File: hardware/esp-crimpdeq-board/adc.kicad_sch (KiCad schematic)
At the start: 13 parts, among them IC1 ADS1235IRHBT, IC3 ADS1230IPWR

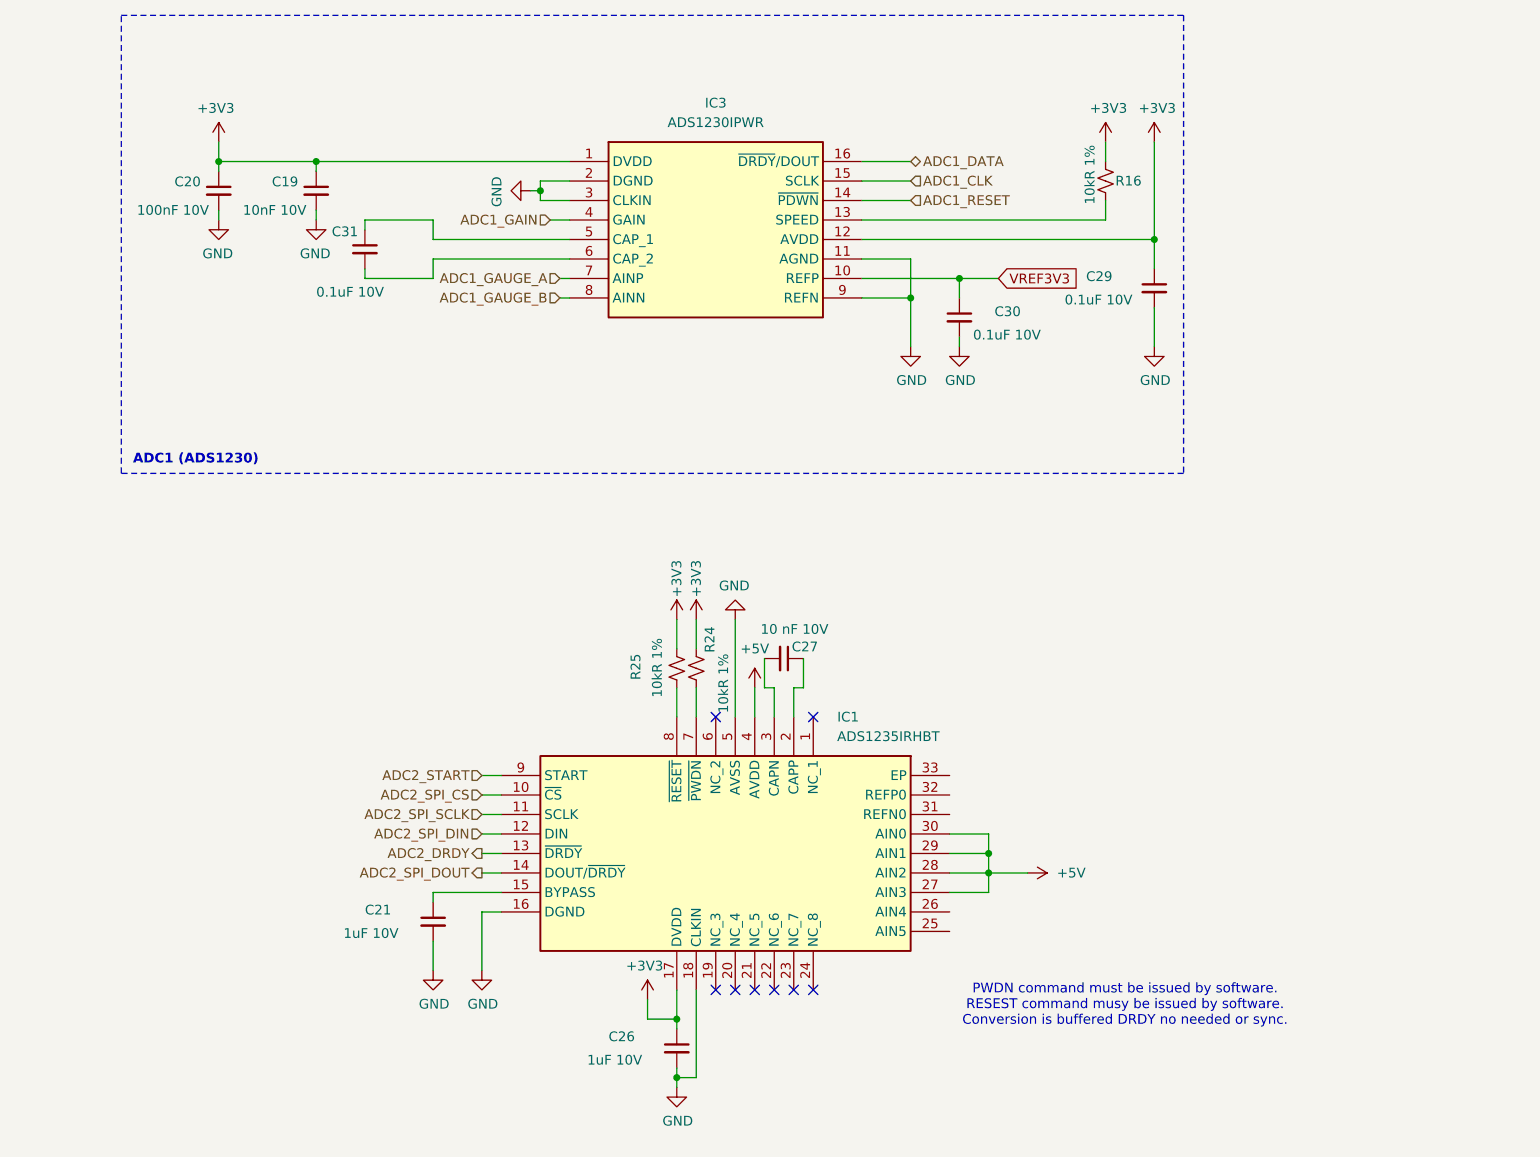
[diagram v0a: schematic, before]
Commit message: Cleaned schematic
- Pending connectors
- Pending BOM and footprints review
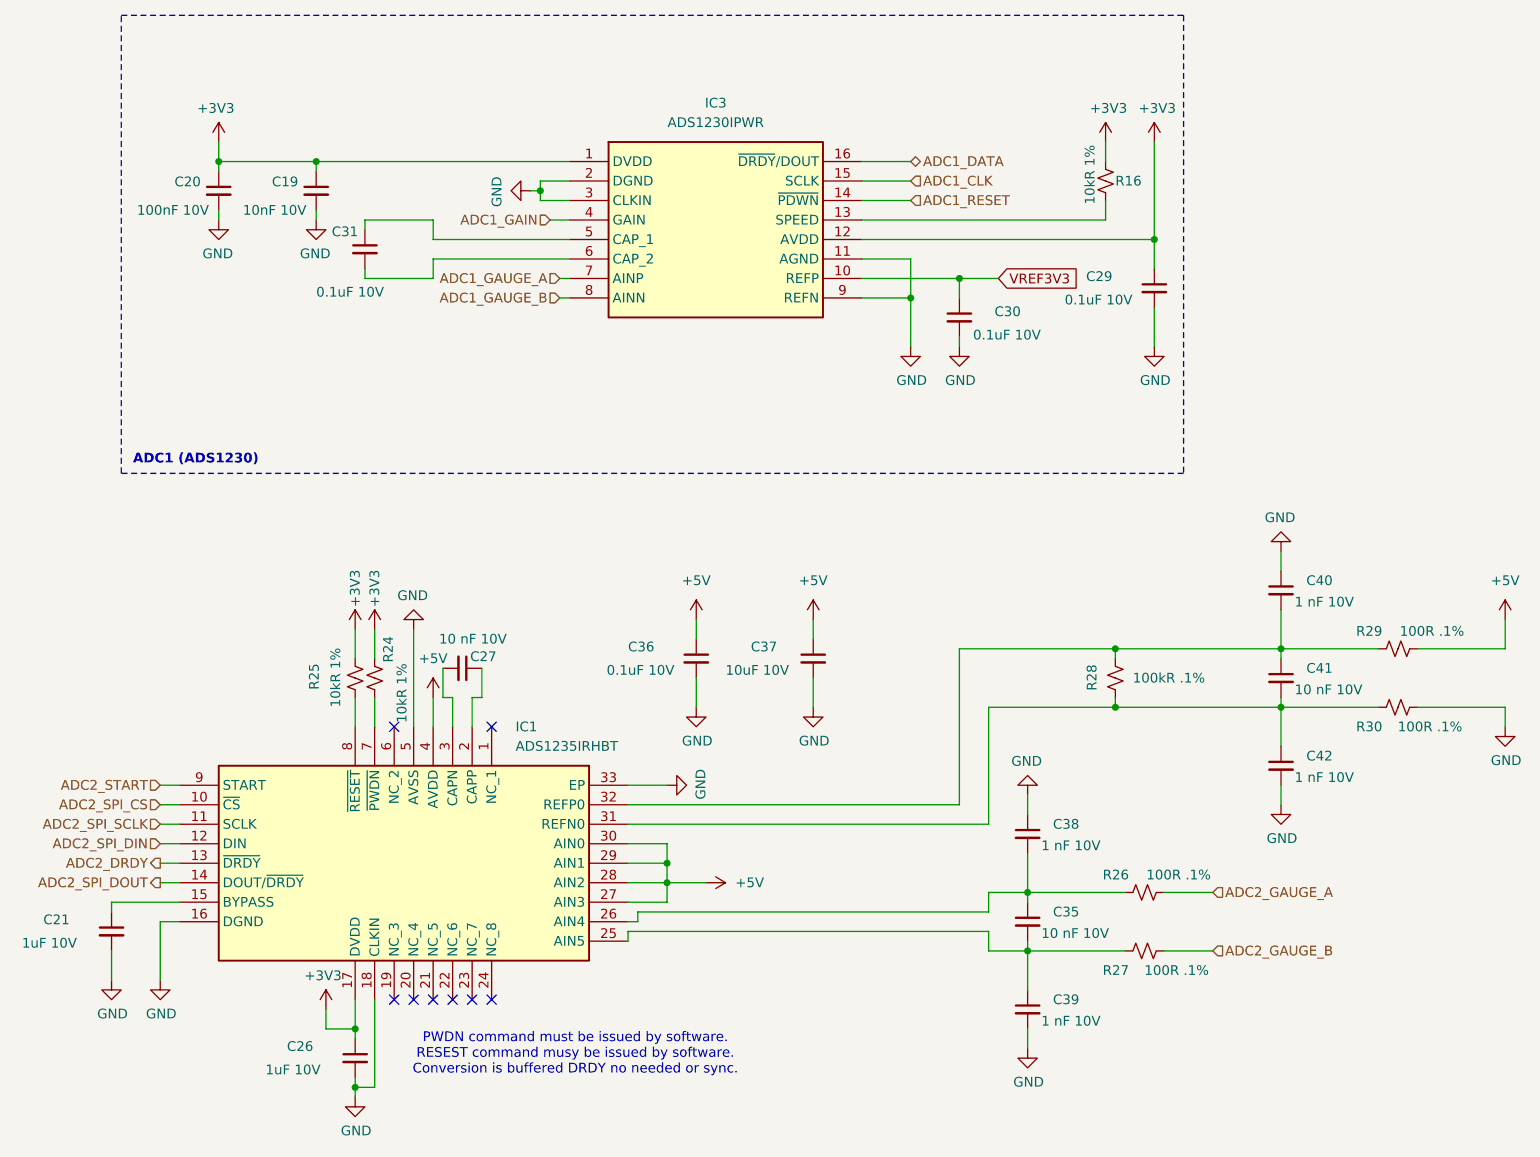
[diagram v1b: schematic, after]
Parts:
- added C35, C41: 10 nF 10V, Capacitor_SMD:C_0402_1005Metric, symbol Device:C_Small
- added C36: 0.1uF 10V, Capacitor_SMD:C_0402_1005Metric, symbol Device:C_Small
- added C37: 10uF 10V, Capacitor_SMD:C_0402_1005Metric, symbol Device:C_Small
- added C38, C39, C40, C42: 1 nF 10V, Capacitor_SMD:C_0402_1005Metric, symbol Device:C_Small
- added R26, R27, R29, R30: 100R .1%, Resistor_SMD:R_0402_1005Metric, symbol Device:R_Small_US
- added R28: 100kR .1%, Resistor_SMD:R_0402_1005Metric, symbol Device:R_Small_US
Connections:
- net +5V: now also C36.1, C37.1, R29.2
- net GND: now also IC1.33 (EP), C36.2, C37.2, C38.1, C39.2, C40.1, C42.2, R30.2
- net at IC1.25 (AIN5): now also C35.2, C39.1, R27.1
- net at IC1.26 (AIN4): now also C35.1, C38.2, R26.1
- net at IC1.31 (REFN0): now also C41.2, C42.1, R28.1, R30.1
- net at IC1.32 (REFP0): now also C40.2, C41.1, R28.2, R29.1
- new net ADC2_GAUGE_A: R26.2
- new net ADC2_GAUGE_B: R27.2
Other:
- moved on the sheet: C21, C26, C27, IC1, R24, R25
